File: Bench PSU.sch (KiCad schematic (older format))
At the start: 0 parts

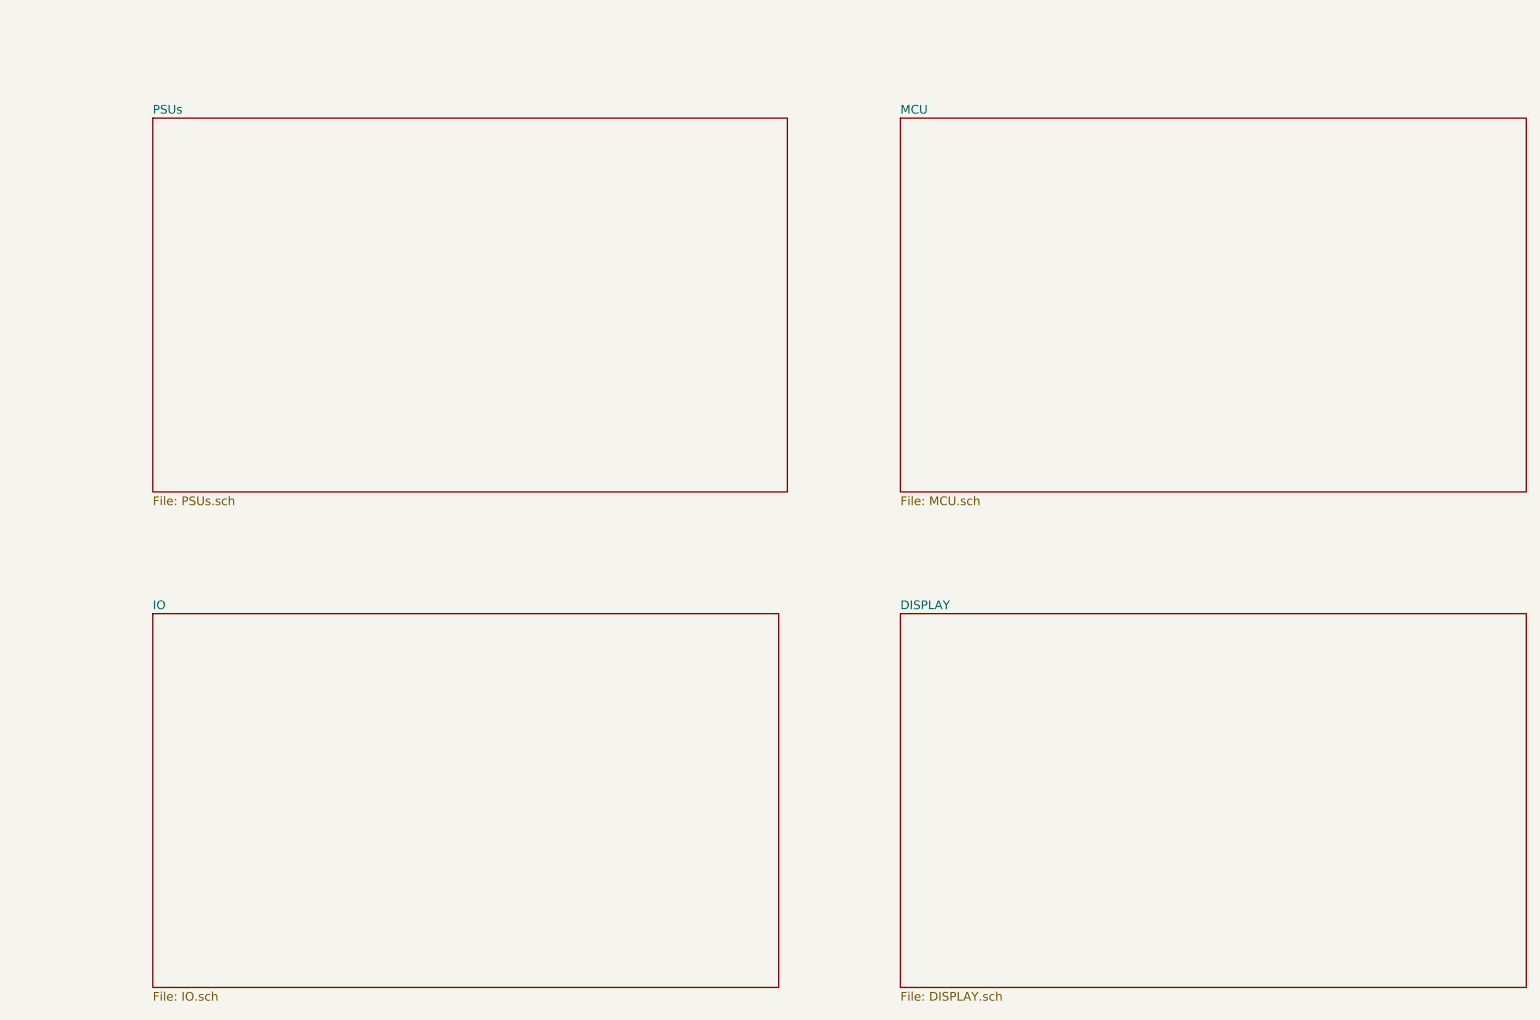
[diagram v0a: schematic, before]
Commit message: added additional IO expanders
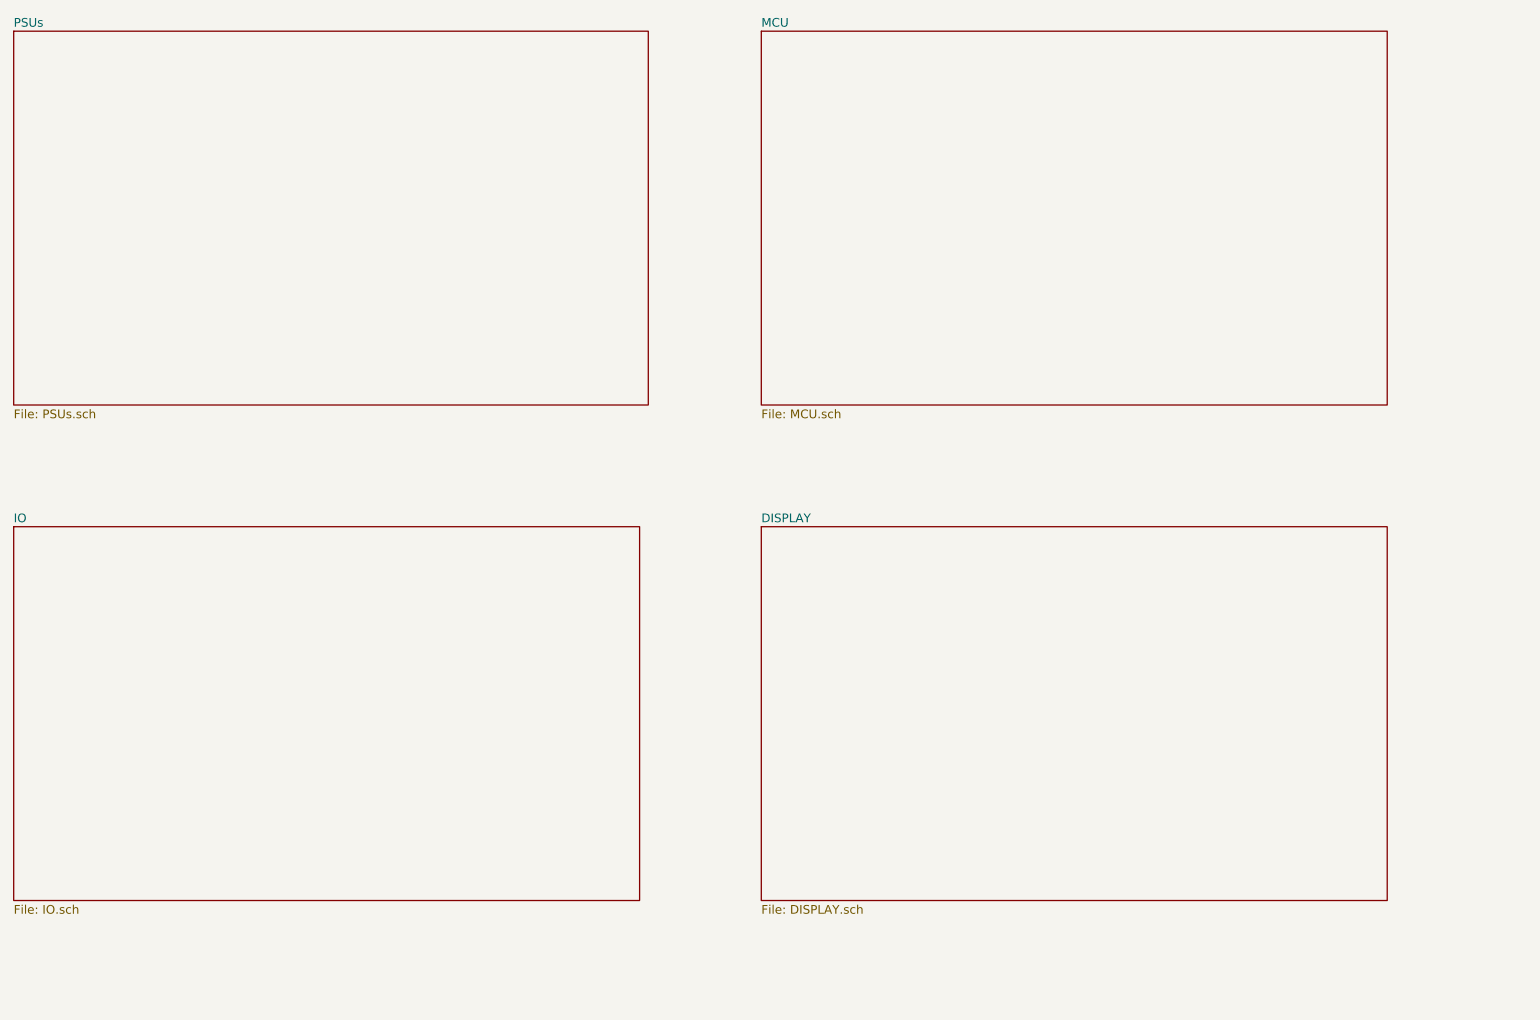
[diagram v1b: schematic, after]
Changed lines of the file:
@@
 $EndDescr
 $Sheet
-S 1850 1400 3650 2150
+S 1050 900  3650 2150
 U 604D3BA3
 F0 "PSUs" 50
@@
 $EndSheet
 $Sheet
-S 6150 1400 3600 2150
+S 5350 900  3600 2150
 U 604D4533
 F0 "MCU" 50
@@
 $EndSheet
 $Sheet
-S 1850 4250 3600 2150
+S 1050 3750 3600 2150
 U 604E5285
 F0 "IO" 50
@@
 $EndSheet
 $Sheet
-S 6150 4250 3600 2150
+S 5350 3750 3600 2150
 U 6096B205
 F0 "DISPLAY" 50

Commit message: Replaced digital pots with analog, removed spi bus too as no longer needed
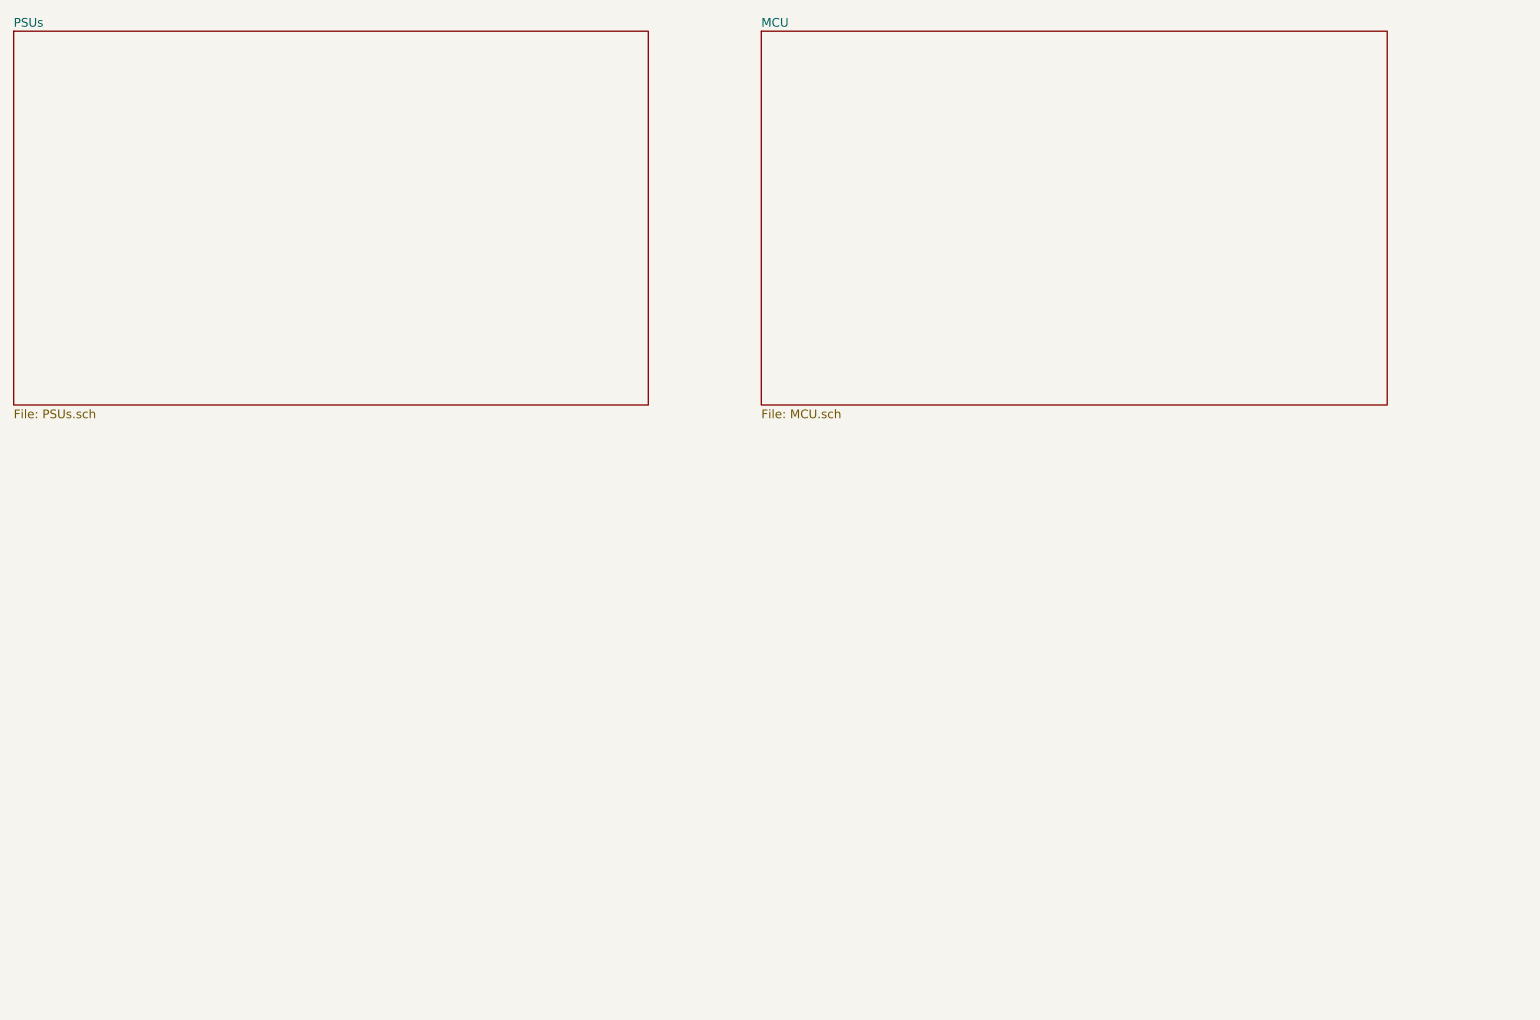
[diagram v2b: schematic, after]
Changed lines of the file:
@@
 $Descr A4 11693 8268
 encoding utf-8
-Sheet 1 5
+Sheet 1 3
 Title ""
 Date ""
@@
 F1 "MCU.sch" 50
 $EndSheet
-$Sheet
-S 1050 3750 3600 2150
-U 604E5285
-F0 "IO" 50
-F1 "IO.sch" 50
-$EndSheet
-$Sheet
-S 5350 3750 3600 2150
-U 6096B205
-F0 "DISPLAY" 50
-F1 "DISPLAY.sch" 50
-$EndSheet
 $EndSCHEMATC
